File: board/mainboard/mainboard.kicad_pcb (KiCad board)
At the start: 2 copper layers, 36 parts, among them J1 QWIIC, J2 QWIIC, J3 UPDI, U1 ATMEGA808, U2 Si4463, U3 BME280, U4 MAX-M8C, U5 TPS613221A

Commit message: latest PCB design update (will commit better henceforth)
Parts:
- added AE1: Antenna_Dipole, Dipole:AE_Pad, B.Cu at (156.2, 73.7)
- added AE2: 1575AT54A0100, 1575AT54:Johanson_AT54, F.Cu at (145.4, 63.5)
- added BT1: AAA, Battery:BatteryHolder_Keystone_2466_1xAAA, B.Cu at (153.1, 99.1)
- added H1: M2, MountingHole:MountingHole_2.2mm_M2, F.Cu at (104.1, 63.5)
- added H1: M2, MountingHole:MountingHole_2.2mm_M2, F.Cu at (157.5, 88.9)
- added H1: M2, MountingHole:MountingHole_2.2mm_M2, F.Cu at (137.2, 88.9)
- added H1: M2, MountingHole:MountingHole_2.2mm_M2, F.Cu at (157.5, 63.5)
- added H1: M2, MountingHole:MountingHole_2.2mm_M2, F.Cu at (104.1, 109.2)
- added H1: M2, MountingHole:MountingHole_2.2mm_M2, F.Cu at (124.5, 109.2)
- added H1: M2, MountingHole:MountingHole_2.2mm_M2, F.Cu at (157.5, 109.2)
- added H1: M2, MountingHole:MountingHole_2.2mm_M2, F.Cu at (124.5, 88.9)
- added H1: M2, MountingHole:MountingHole_2.2mm_M2, F.Cu at (104.1, 88.9)
- added H1: M2, MountingHole:MountingHole_2.2mm_M2, F.Cu at (137.2, 109.2)
- added J4: RFShield_OnePiece, RF_Shielding:Wuerth_36103205_20x20mm, B.Cu at (120.7, 73.7)
- added SW1: SAJ1-SNC, SAJ13:SAJ1______N88SNCPT_, F.Cu at (130.8, 104.8)
- added Y1: 30MHz, Crystal:Crystal_SMD_3225-4Pin_3.2x2.5mm, B.Cu at (116.0, 80.0)
- C1, C13, C14, C2, C6, C7: footprint Capacitor_SMD:C_0603_1608Metric_Pad1.08x0.95mm_HandSolder -> Capacitor_SMD:C_0402_1005Metric
- C10, C9: footprint Capacitor_SMD:C_0603_1608Metric_Pad1.08x0.95mm_HandSolder -> Capacitor_SMD:C_0402_1005Metric; moved to B.Cu
- C11, C12: footprint Capacitor_SMD:C_0805_2012Metric_Pad1.18x1.45mm_HandSolder -> Capacitor_SMD:C_0603_1608Metric
- C3, C4, C5, C8: footprint Capacitor_SMD:C_0603_1608Metric_Pad1.08x0.95mm_HandSolder -> Capacitor_SMD:C_0603_1608Metric; moved to B.Cu
- D1: footprint LED_SMD:LED_0603_1608Metric_Pad1.05x0.95mm_HandSolder -> LED_SMD:LED_0603_1608Metric
- FB1: footprint Inductor_SMD:L_0805_2012Metric_Pad1.05x1.20mm_HandSolder -> Inductor_SMD:L_0805_2012Metric
- J3: footprint Connector_PinHeader_2.54mm:PinHeader_1x03_P2.54mm_Vertical -> Connector_PinHeader_2.54mm:PinHeader_1x03_P2.54mm_Horizontal
- L1, L2, L3, L4: footprint Inductor_SMD:L_0603_1608Metric_Pad1.05x0.95mm_HandSolder -> Inductor_SMD:L_0603_1608Metric; moved to B.Cu
- L5: value 620n -> 390n; footprint Inductor_SMD:L_1008_2520Metric_Pad1.43x2.20mm_HandSolder -> Inductor_SMD:L_0603_1608Metric; moved to B.Cu
- R1: footprint Resistor_SMD:R_0603_1608Metric_Pad0.98x0.95mm_HandSolder -> Resistor_SMD:R_0603_1608Metric; moved to B.Cu
- R2, R3, R4, R5: footprint Resistor_SMD:R_0603_1608Metric_Pad0.98x0.95mm_HandSolder -> Resistor_SMD:R_0603_1608Metric
- U2, U3: moved to B.Cu
- moved J2 142.6 mm to (147.3, 108.5)
- moved U4 134.1 mm to (142.1, 78.7), turned to 90 degrees
- moved J3 126.0 mm to (152.6, 46.4), turned to -90 degrees
- moved L6 123.5 mm to (135.6, 99.3), turned to 90 degrees
- moved C11 123.1 mm to (133.0, 93.2)
- moved FB1 118.5 mm to (122.9, 93.0), turned to 180 degrees
- moved U1 118.2 mm to (118.1, 99.1), turned to 90 degrees
- moved U5 118.2 mm to (133.3, 95.8), turned to 180 degrees
- moved J1 115.0 mm to (114.3, 108.5)
- moved C7 113.3 mm to (145.4, 85.8), turned to 90 degrees
- moved C12 112.4 mm to (133.0, 91.7)
- moved C6 110.5 mm to (144.3, 85.8), turned to 90 degrees
- moved L5 108.7 mm to (129.0, 76.7), turned to 90 degrees
- moved L4 104.5 mm to (126.0, 72.9), turned to 90 degrees
- moved C14 103.3 mm to (119.7, 93.0)
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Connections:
- net -BATT renamed GND
- L6 pad 1: +BATT -> Net-(L6-Pad1)
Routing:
- net +3V3: track 0.00 -> 91.9 mm, vias 0 -> 2
- net Net-(BT1-Pad1): track 0.00 -> 33.0 mm
- net /SDA2: track 0.00 -> 28.8 mm
- net /SCL2: track 0.00 -> 28.8 mm
- net /UATX: track 0.00 -> 24.7 mm
- net /UARX: track 0.00 -> 24.6 mm
- net Net-(C13-Pad2): track 0.00 -> 16.6 mm, vias 0 -> 2
- net Net-(C8-Pad2): track 0.00 -> 11.2 mm
- net Net-(AE2-Pad1): track 0.00 -> 8.44 mm
- net Net-(AE1-Pad2): track 0.00 -> 6.83 mm
- net GND: track 0.00 -> 5.68 mm, vias 0 -> 84
- net Net-(L6-Pad1): track 0.00 -> 5.09 mm
- net /SDA1: track 0.00 -> 4.74 mm
- net Net-(U2-Pad16): track 0.00 -> 4.11 mm
- net /SCL1: track 0.00 -> 3.10 mm
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- added copper zone on B.Cu, net GND
- added copper zone on F.Cu, net GND
- added copper zone on F.Cu, net Net-(AE2-Pad1)
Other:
- board outline added: 58.4 x 50.8 mm

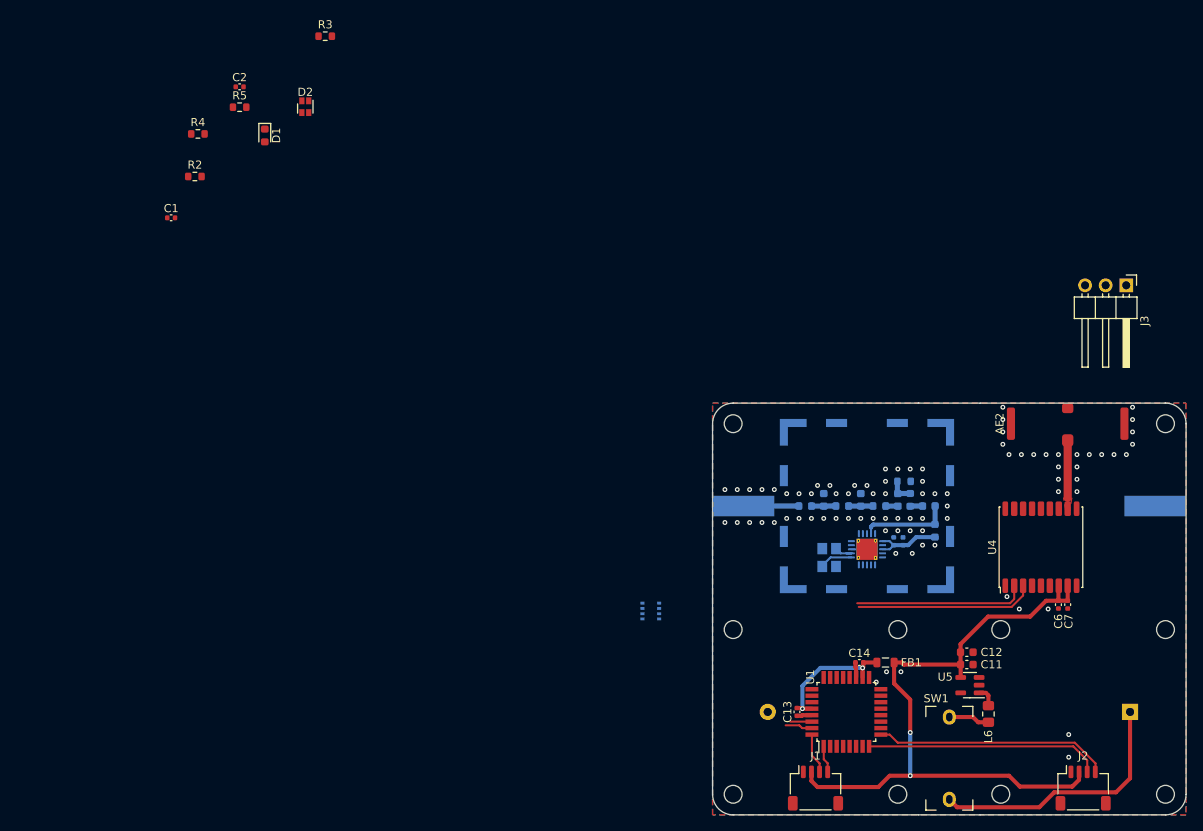
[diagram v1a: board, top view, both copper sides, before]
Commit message: export mainboard VRML
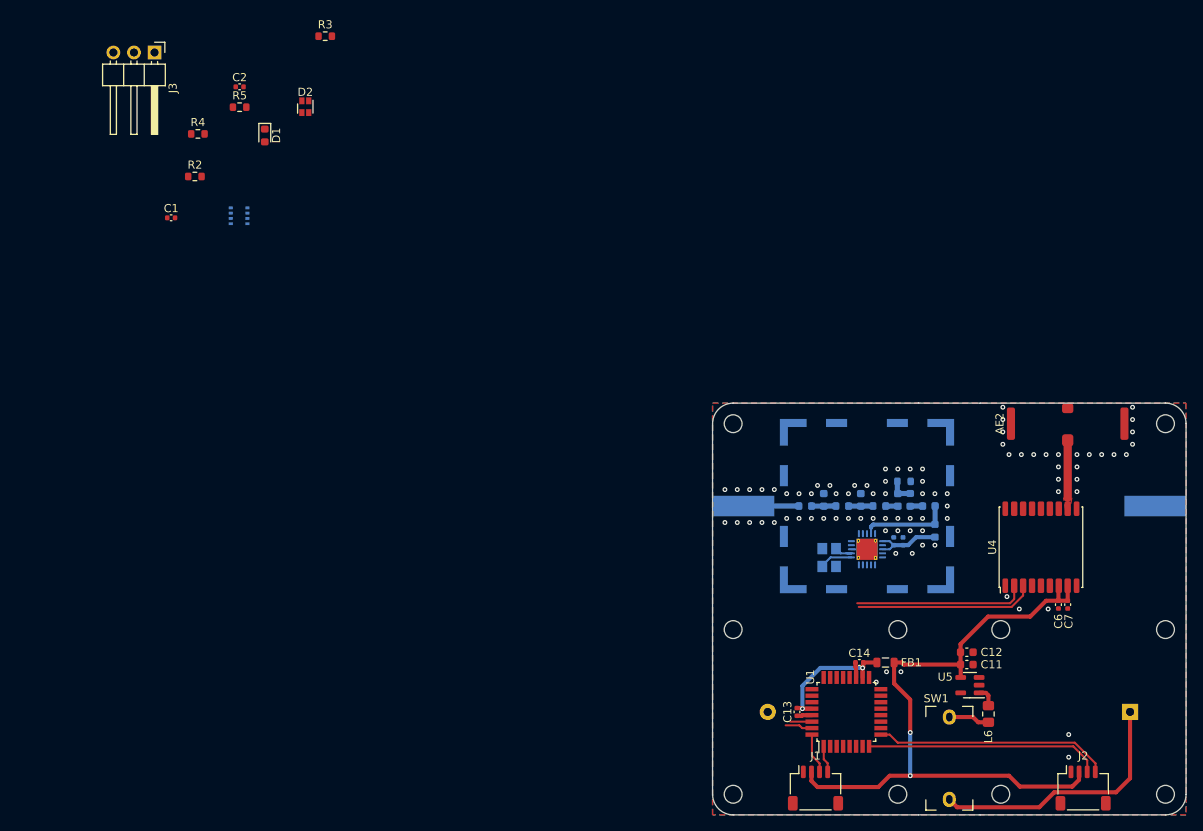
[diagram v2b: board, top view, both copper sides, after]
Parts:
- moved J3 123.3 mm to (32.8, 17.7)
- moved U3 70.4 mm to (43.2, 37.8)
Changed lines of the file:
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@@
   )
   (footprint "Connector_PinHeader_2.54mm:PinHeader_1x03_P2.54mm_Horizontal" (layer "F.Cu")
-    (at 152.639 46.425 -90)
+    (at 32.751 17.702 -90)
     (descr "Through hole angled pin header, 1x03, 2.54mm pitch, 6mm pin length, single row")
     (tags "Through hole angled pin header THT 1x03 2.54mm single row")
@@
   )
   (footprint "Package_LGA:Bosch_LGA-8_2.5x2.5mm_P0.65mm_ClockwisePinNumbering" (layer "B.Cu")
-    (at 93.98 86.614 -90)
+    (at 43.18 37.846 -90)
     (descr "LGA-8")
     (tags "lga land grid array")

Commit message: completed layouting for mainboard
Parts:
- added C15: 2.2µ, Capacitor_SMD:C_0603_1608Metric, F.Cu at (137.7, 99.6)
- J3: footprint Connector_PinHeader_2.54mm:PinHeader_1x03_P2.54mm_Horizontal -> Connector_PinHeader_2.54mm:PinHeader_1x03_P2.54mm_Vertical; moved to B.Cu
- R2, R4: footprint Resistor_SMD:R_0603_1608Metric -> Resistor_SMD:R_0402_1005Metric
- R3: renamed from R5; footprint Resistor_SMD:R_0603_1608Metric -> Resistor_SMD:R_0402_1005Metric
- R5: renamed from R3; footprint Resistor_SMD:R_0603_1608Metric -> Resistor_SMD:R_0402_1005Metric
- U3: moved to F.Cu
- moved J3 109.7 mm to (103.5, 101.6), turned to 0 degrees
- moved C2 105.7 mm to (108.6, 105.0)
- moved C1 97.0 mm to (106.6, 103.4), turned to -90 degrees
- moved U3 92.2 mm to (108.6, 102.9), turned to 0 degrees
- moved R4 87.4 mm to (107.2, 81.3), turned to 180 degrees
- moved R3 86.4 mm to (107.2, 82.5), turned to 180 degrees
- moved R2 86.1 mm to (107.2, 83.8), turned to 180 degrees
- moved R5 83.6 mm to (107.2, 80.0), turned to 180 degrees
- moved D1 80.4 mm to (104.1, 83.8), turned to 180 degrees
- moved D2 77.0 mm to (104.1, 80.4), turned to -90 degrees
- moved BT1 44.6 mm to (108.5, 99.1), turned to 0 degrees
- moved C12 5.49 mm to (129.0, 95.5), turned to -90 degrees
- moved C11 3.33 mm to (130.6, 95.5), turned to -90 degrees
- moved U5 0.07 mm to (133.3, 95.7)
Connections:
- BT1 pad 1: Net-(BT1-Pad1) -> /+VIN
- J3 pad 1: /+5V -> /+VIN
- SW1 pad 2: Net-(BT1-Pad1) -> /+VIN
- U1 pad 20: unconnected-(U1-Pad20) -> /UATX
- U1 pad 21: unconnected-(U1-Pad21) -> /UARX
- U1 pad 22: unconnected-(U1-Pad22) -> /~{L_{ST-R}}
- U1 pad 23: unconnected-(U1-Pad23) -> /~{L_{ST-G}}
- U1 pad 24: unconnected-(U1-Pad24) -> /~{L_{ST-B}}
- U1 pad 25: unconnected-(U1-Pad25) -> /~{L_{ON}}
- U1 pad 30: /UATX -> /~{CS}2
- U1 pad 31: /UARX -> /~{CS}1
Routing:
- net +3V3: track 91.9 -> 146.8 mm, vias 2 -> 4
- net /SCK: track 0.03 -> 35.1 mm, vias 0 -> 2
- net /+VIN: track 0.00 -> 34.7 mm
- net Net-(BT1-Pad1): track 33.0 -> 0.00 mm
- net /MOSI: track 0.00 -> 32.6 mm, vias 0 -> 2
- net /MISO: track 0.00 -> 32.3 mm, vias 0 -> 2
- net /~{CS}2: track 0.00 -> 22.6 mm, vias 0 -> 1
- net /~{L_{ST-R}}: track 0.00 -> 19.0 mm
- net /~{L_{ST-G}}: track 0.00 -> 17.8 mm
- net /~{L_{ON}}: track 0.00 -> 17.6 mm
- net /~{L_{ST-B}}: track 0.00 -> 16.8 mm
- net /UPDI: track 0.00 -> 10.9 mm
- net /UATX: track 24.7 -> 31.0 mm
- net /~{CS}1: track 0.00 -> 6.18 mm
- net /UARX: track 24.6 -> 30.6 mm
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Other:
- board text added: "HABSAT TRACKER (BLOCK I)"
- board text added: "UPDI"
